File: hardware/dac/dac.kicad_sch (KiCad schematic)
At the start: 18 parts

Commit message: DAC layout almost done
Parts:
- removed C?: 0.1uF, symbol Device:C_Small
- removed U? (x3): 74LS139, symbol 74xx:74LS139
- removed U? (x2): 74LS04, symbol 74xx:74LS04
- added BT1: Battery_Cell, Connector_PinHeader_2.54mm:PinHeader_1x02_P2.54mm_Vertical, symbol Device:Battery_Cell
- added C11, C16, C2, C3, C4, C5, C6, C7, C8, C9: 0.1uF, Capacitor_THT:C_Disc_D3.4mm_W2.1mm_P2.50mm, symbol Device:C_Small
- added C14, C15: 33uF, Capacitor_THT:CP_Radial_D5.0mm_P2.00mm, symbol Device:C_Polarized_Small
- added C17, C18: 3.3uF 10V, Capacitor_THT:CP_Radial_D5.0mm_P2.50mm, symbol Device:C_Polarized_Small
- added D1, D2, D3: LED, LED_THT:LED_D3.0mm, symbol Device:LED
- added H1, H2, H3, H4: MountingHole, MountingHole:MountingHole_3.2mm_M3, symbol Mechanical:MountingHole
- added IC1: EC1110120201_with_knurled_SHAFT, ShaftEnc:EC1110120201withknurledSHAFT, symbol EC1110120201_with_knurled_SHAF:EC1110120201_with_knurled_SHAFT
- added J1, J7: Conn_01x04, Connector_PinHeader_2.54mm:PinHeader_1x04_P2.54mm_Vertical, symbol Connector_Generic:Conn_01x04
- added J4: Conn_02x08_Odd_Even, Connector_PinHeader_2.54mm:PinHeader_2x08_P2.54mm_Vertical, symbol Connector_Generic:Conn_02x08_Odd_Even
- added J5: Conn_01x02, Connector_PinHeader_2.54mm:PinHeader_1x02_P2.54mm_Vertical, symbol Connector_Generic:Conn_01x02
- added Q1: Q_PNP_BCE, Package_TO_SOT_THT:TO-92, symbol Device:Q_PNP_BCE
- added R1, R2, R3: R_US, Resistor_THT:R_Axial_DIN0207_L6.3mm_D2.5mm_P10.16mm_Horizontal, symbol Device:R_US
- added R4, R7: 10k, Resistor_THT:R_Axial_DIN0207_L6.3mm_D2.5mm_P10.16mm_Horizontal, symbol Device:R_US
- added R5, R6: 1k, Resistor_THT:R_Axial_DIN0207_L6.3mm_D2.5mm_P10.16mm_Horizontal, symbol Device:R_US
- added SW1, SW2: SW_SPST, Connector_PinHeader_2.54mm:PinHeader_1x02_P2.54mm_Vertical, symbol Switch:SW_SPST
- added U1: 74HC4040, Package_DIP:DIP-16_W7.62mm, symbol 4xxx:4040
- added unit 2 of U2
- added U3: 74LS174, Package_DIP:DIP-16_W7.62mm, symbol 74xx:74LS174
- added U5: 74LS138, Package_DIP:DIP-16_W7.62mm, symbol 74xx:74LS138
- added U6: DS1306, Package_DIP:DIP-16_W7.62mm, symbol DS1306:DS1306
- added U9: MAX503, Package_DIP:DIP-24_W7.62mm, symbol MAX530:MAX530
- added X1: 4.9152MHz, Oscillator:Oscillator_DIP-8, symbol Oscillator:CXO_DIP8
- added Y1: 32.768 kHz, Crystal:Crystal_C26-LF_D2.1mm_L6.5mm_Horizontal, symbol Device:Crystal
- C1, C10: renamed from C?; footprint (none) -> Capacitor_THT:C_Disc_D3.4mm_W2.1mm_P2.50mm; CatNo (none) -> 399-9859-1-ND
- C12, C13: renamed from C?; value C_Small -> 0.1uF; footprint (none) -> Capacitor_THT:C_Disc_D3.4mm_W2.1mm_P2.50mm; CatNo (none) -> 399-9859-1-ND
- J2, J3: renamed from J?; footprint (none) -> Connector_PinHeader_2.54mm:PinHeader_2x08_P2.54mm_Vertical
- J6: renamed from J?; footprint (none) -> Connector_PinHeader_2.54mm:PinHeader_1x04_P2.54mm_Horizontal
- U2: renamed from U?; footprint (none) -> Package_DIP:DIP-14_W7.62mm; CatNo (none) -> 296-1633-5-ND
- U4: renamed from U?; value 74LS245 -> 74HCT245; footprint (none) -> Package_DIP:DIP-20_W7.62mm; CatNo (none) -> 296-1612-5-ND
- U7: renamed from U?; footprint (none) -> Package_DIP:DIP-40_W15.24mm; CatNo (none) -> 2156-HD3-6402C-9-ND
- U8: renamed from U?; value MAX530 -> MAX503; footprint (none) -> Package_DIP:DIP-24_W7.62mm; CatNo (none) -> MAX503CNG+-ND
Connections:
- net +5V: now also U7.34 (CRL), U7.35 (PI), U7.37 (CLS2), U7.38 (CLS1), U8.15 (nCLR), U8.23 (VDD), C16.1, C17.1, C2.1, C3.1, C4.1, C6.1, C7.1, C9.1, D1.2 (A), D2.2 (A), D3.2 (A), J1.1 (Pin_1), Q1.3 (E), R7.2, U1.16 (VDD), U2.4, U3.16 (VCC), U5.16 (VCC), U5.6 (E3), U6.14 (VCCIF), U6.16 (VCC), U6.9 (SERMODE), U9.15 (nCLR), U9.23 (VDD), X1.8 (Vcc)
- net A0: now also U2.5
- net BD0: now also U8.24 (D0/D8), U3.3 (D0), U6.12 (SDI), U9.24 (D0/D8); no longer U7.38 (CLS1)
- net BD1: now also U8.1 (D1/D9), U3.4 (D1), U9.1 (D1/D9); no longer U7.37 (CLS2)
- net BD2: now also U8.2 (D2/D10), U3.6 (D2), U9.2 (D2/D10); no longer U7.36 (SBS)
- net BD3: now also U8.3 (D3/D11), U3.11 (D3), U9.3 (D3/D11); no longer U7.39 (EPE)
- net BD4: now also U8.4 (D4), U3.13 (D4), U9.4 (D4); no longer U7.35 (PI)
- net BD5: now also U8.5 (D5), U3.14 (D5), U9.5 (D5)
- net BD6: now also U8.6 (D6), U9.6 (D6)
- net BD7: now also U8.7 (D7), U9.7 (D7)
- net GND: now also J6.4 (Pin_4), U7.36 (SBS), U7.39 (EPE), U8.11 (nCS), U8.12 (DGND), U8.14 (AGND), U8.16 (nLDAC), U8.17 (REFGND), BT1.2 (-), C11.2, C14.2, C15.2, C16.2, C17.2, C18.1, C2.2, C3.2, C4.2, C5.2, C6.2, C7.2, C8.2, C9.2, IC1.C1 (WIPER), IC1.D1 (COM), J1.2 (Pin_2), J1.4 (Pin_4), J7.2 (Pin_2), J7.4 (Pin_4), SW1.1 (A), SW2.1 (A), U1.11 (Reset), U1.8 (VSS), U3.8 (GND), U5.5 (E2), U5.8 (GND), U6.1 (VCC2), U6.8 (GND), U9.11 (nCS), U9.16 (nLDAC), X1.4 (GND)
- net KD0: now also IC1.A1 (CCW)
- net KD1: now also IC1.B1 (CW)
- net KD2: now also IC1.E1 (NO)
- net KD3: now also SW1.2 (B)
- net KD4: now also SW2.2 (B); no longer J3.5 (Pin_5)
- net KD5: now also U6.13 (SDO)
- net KQ0: now also U5.1 (A0)
- net KQ1: now also U5.3 (A2)
- net KQ2: now also R4.1, R7.1
- net KQ3: now also U7.21 (MR)
- net KQ4: now also U6.10 (CE)
- net RXD: now also J6.2 (Pin_2)
- net TXD: now also J6.3 (Pin_3)
- net nLED1: now also U5.4 (E1)
- net nLED2: now also U6.11 (SCLK)
- net at U7.23 (nTBRL): now also U5.14 (O1)
- net at U7.18 (nDRR), U7.4 (RRD): now also U5.15 (O0)
- net at U7.16 (SFD): now also U5.13 (O2)
- net nDACX: now reaches U8.10 (nWR)
- net nDACX: now also U5.12 (O3)
- net at U8.13 (REFIN): now also U8.18 (REFOUT), U8.22 (ROFS), C14.1
- net -5V: now reaches U8.19 (VSS)
- net -5V: now also C11.1, C18.2, C5.1, C8.1, J1.3 (Pin_3), J5.2 (Pin_2), U9.19 (VSS)
- net at U8.20 (VOUT): now also U8.21 (RFB), R5.1
- net BA0: now reaches U8.8 (A0)
- net BA0: now also U8.9 (A1), U2.6, U5.2 (A1), U9.8 (A0), U9.9 (A1)
- net CLK16X: now reaches U7.17 (RRC)
- net CLK16X: now also U7.40 (TRC), J4.10 (Pin_10), J4.12 (Pin_12), J4.14 (Pin_14), J4.16 (Pin_16), J4.2 (Pin_2), J4.4 (Pin_4), J4.6 (Pin_6), J4.8 (Pin_8)
- new net: D1.1 (K), R1.2
- new net: D3.1 (K), R3.2
- new net: J5.1 (Pin_1), Q1.2 (C)
- new net: C15.1, U9.13 (REFIN), U9.18 (REFOUT), U9.22 (ROFS)
- new net: Q1.1 (B), R4.2
- new net: R6.1, U9.20 (VOUT), U9.21 (RFB)
- new net: BT1.1 (+), U6.2 (VBAT)
- new net: U6.3 (X1), Y1.1
- new net: U6.4 (X2), Y1.2
- new net: D2.1 (K), R2.2
- new net: U1.10 (CLK), X1.5 (OUT)
- new net: U9.12 (DGND), U9.14 (AGND), U9.17 (REFGND)
- new net B1200: J4.11 (Pin_11), U1.13 (Q7)
- new net B19200: J4.3 (Pin_3), U1.5 (Q3)
- new net B2400: J4.9 (Pin_9), U1.4 (Q6)
- new net B300: J4.15 (Pin_15), U1.14 (Q9)
- new net B38400: J4.1 (Pin_1), U1.6 (Q2)
- new net B4800: J4.7 (Pin_7), U1.2 (Q5)
- new net B600: J4.13 (Pin_13), U1.12 (Q8)
- new net B9600: J4.5 (Pin_5), U1.3 (Q4)
- new net LED0: R1.1, U3.2 (Q0)
- new net LED1: R2.1, U3.5 (Q1)
- new net LED2: R3.1, U3.7 (Q2)
- new net LED3: U3.10 (Q3)
- new net LED4: U3.12 (Q4)
- new net LED5: U3.15 (Q5)
- new net X_OUT: J7.1 (Pin_1), R6.2
- new net Y_OUT: J7.3 (Pin_3), R5.2
- new net nDACY: U5.10 (O5), U9.10 (nWR)
- new net nEXP: U3.9 (Cp), U5.7 (O7)
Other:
- note added: "8 bits, no parity 1 stop bit"
- note added: "Baud Rate Generator"
- note added: "CRT Z axis drive"
- note added: "Even: RD Odd: WR"
- note added: "Input Bits: KD0 - encoder A KD1 - encoder B KD2 - encoder SW KD3 - button 1 KD4 - button 2 KD5 - RTC Serial Data KD6 - Spare"
- note added: "Primiary Outputs KQ0 dir H=WR KQ1 dev sel 0 KQ2 Z enable KQ3 UART reset KQ4 RTC CE"
- note added: "RD"
- note added: "Real-Time Clock"
- note added: "Shaft Encoder"
- note added: "Sparkfun BOB-12731 USB - FT232RL"
- note added: "UART"
- note added: "WR"
- note removed: "CTRL LOAD"
- note removed: "FT232 breakout"
- moved on the sheet: C1, C10, J6, U2A, U2E, U8

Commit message: PCB Rev 1 ready to fab?
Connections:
- net +5V: now also U3.1 (~{Mr})
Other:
- note added: "Scope Clock DAQ/Control Interface"
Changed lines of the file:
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@@
     (stroke (width 0) (type default) (color 0 0 0 0))
   )
+  (wire (pts (xy 85.09 191.77) (xy 87.63 191.77))
+    (stroke (width 0) (type default) (color 0 0 0 0))
+  )
   (wire (pts (xy 113.03 181.61) (xy 120.65 181.61))
     (stroke (width 0) (type default) (color 0 0 0 0))
@@
     (effects (font (size 1.27 1.27)) (justify left bottom))
   )
+  (text "Scope Clock DAQ/Control Interface" (at 161.29 180.34 0)
+    (effects (font (size 2.54 2.54)) (justify left bottom))
+  )
   (text "Real-Time Clock" (at 123.19 113.03 0)
     (effects (font (size 1.905 1.905)) (justify left bottom))
@@
     (pin "1")
   )
+  (symbol (lib_id "power:+5V") (at 85.09 191.77 0) (unit 1)
+    (in_bom yes) (on_board yes)
+    (property "Reference" "#PWR?" (id 0) (at 85.09 195.58 0)
+      (effects (font (size 1.27 1.27)) hide)
+    )
+    (property "Value" "+5V" (id 1) (at 81.28 190.5 0))
+    (property "Footprint" "" (id 2) (at 85.09 191.77 0)
+      (effects (font (size 1.27 1.27)) hide)
+    )
+    (property "Datasheet" "" (id 3) (at 85.09 191.77 0)
+      (effects (font (size 1.27 1.27)) hide)
+    )
+    (pin "1")
+  )
   (symbol (lib_id "power:GND") (at 110.49 109.22 0) (unit 1)
     (in_bom yes) (on_board yes)
@@
       (reference "#PWR053") (unit 1) (value "GND") (footprint "")
     )
+    (path "/12f4a369-d6ff-4aa1-ab4f-7a5c25ac096c"
+      (reference "#PWR?") (unit 1) (value "+5V") (footprint "")
+    )
     (path "/7e11c5d6-00d5-4ef8-b7e7-4746244c75fa"

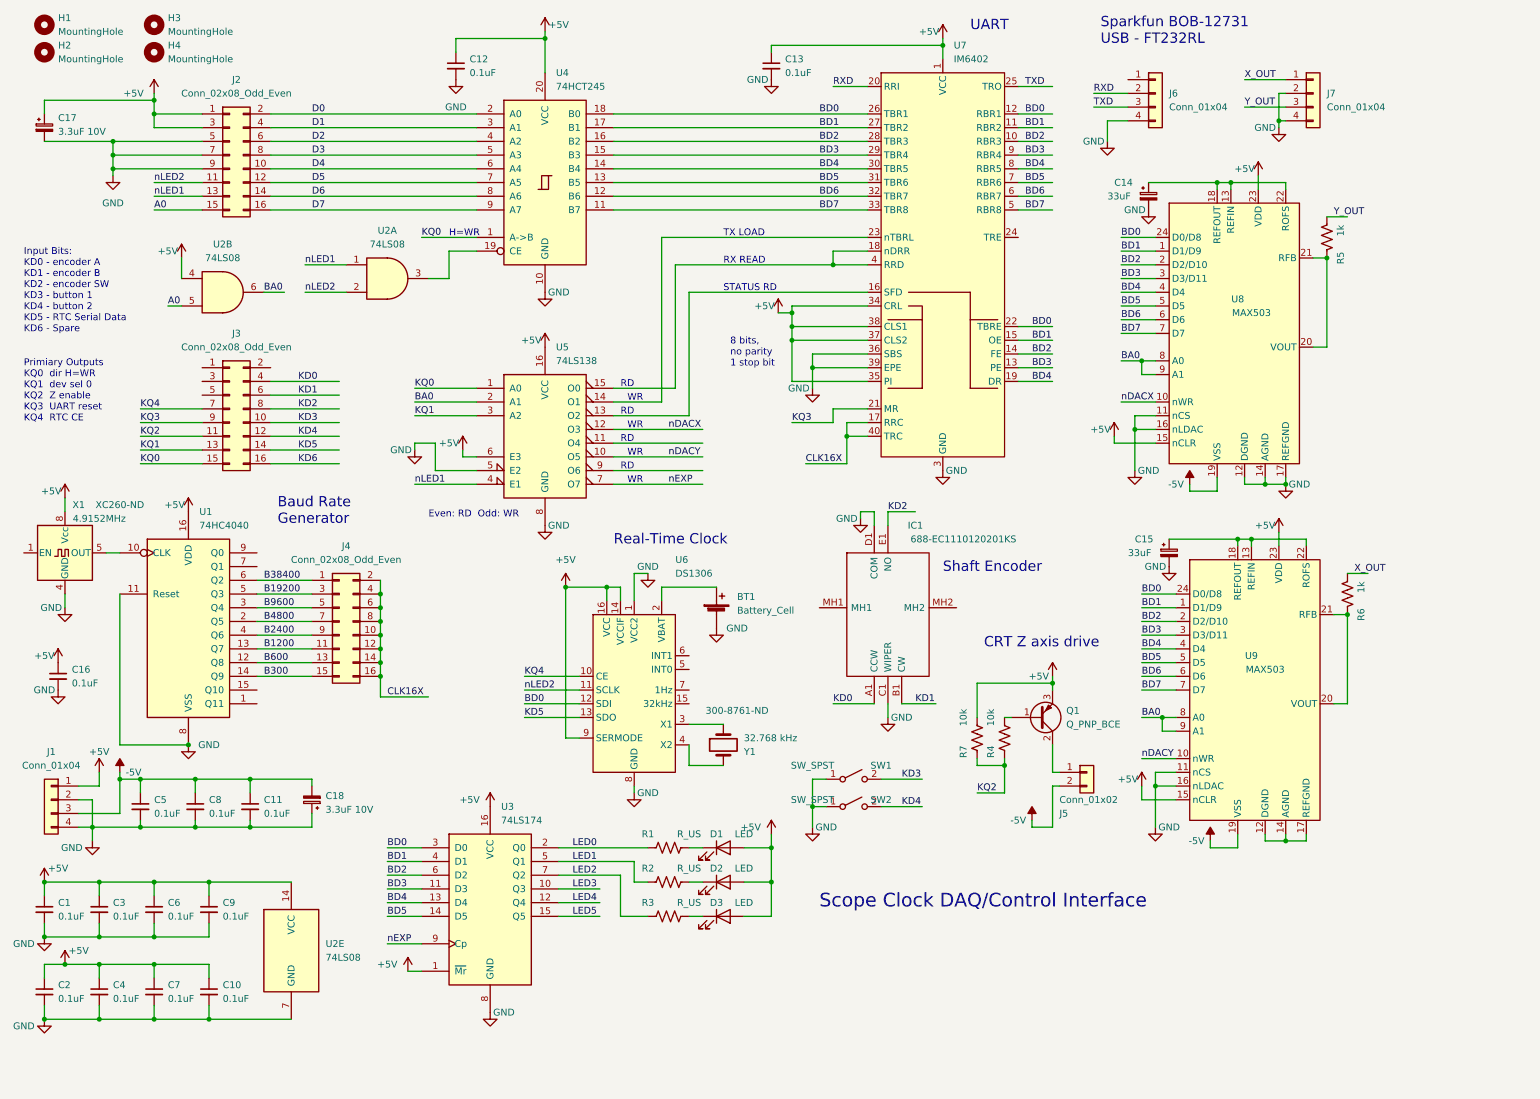
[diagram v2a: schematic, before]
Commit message: working on Rev 2 DAC
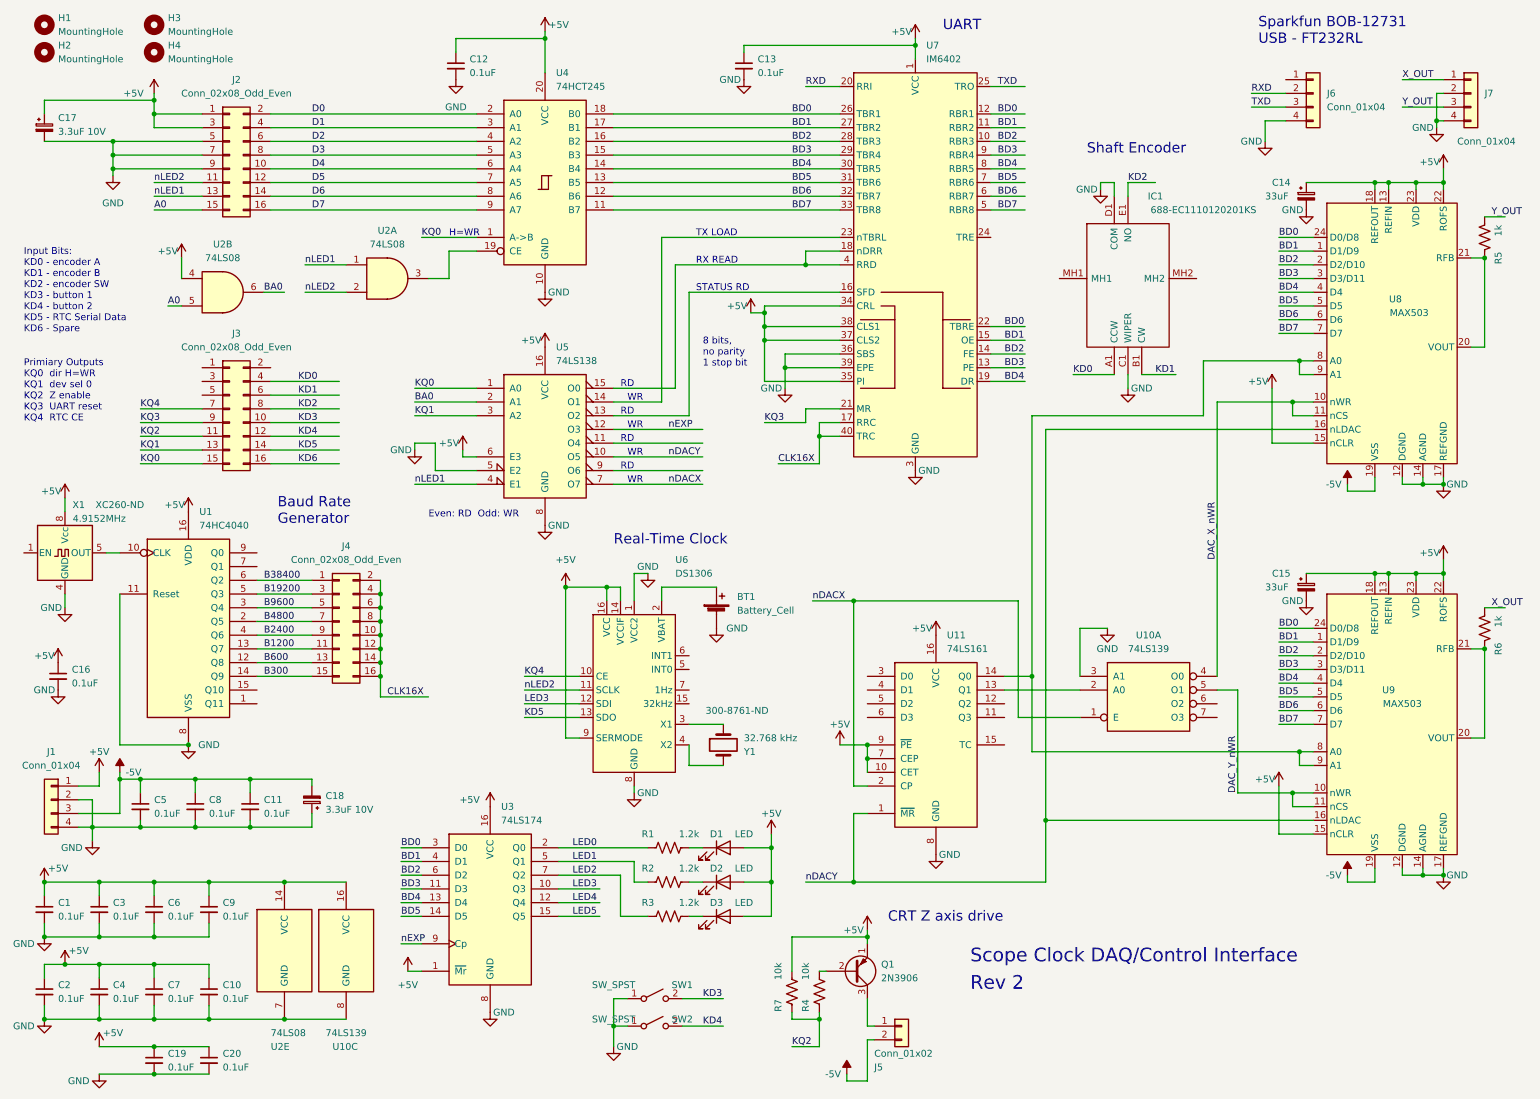
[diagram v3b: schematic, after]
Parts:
- added C19, C20: 0.1uF, Capacitor_THT:C_Disc_D3.4mm_W2.1mm_P2.50mm, symbol Device:C_Small
- added U10: 74LS139, Package_DIP:DIP-16_W7.62mm, symbol 74xx:74LS139
- added U11: 74LS161, Package_DIP:DIP-16_W7.62mm, symbol 74xx:74LS161
- C17, C18: CatNo (none) -> 10-EEU-FC1H3R3HCT-ND
- Q1: value Q_PNP_BCE -> 2N3906; symbol Device:Q_PNP_BCE -> Device:Q_PNP_EBC
- R1, R2, R3: value R_US -> 1.2k
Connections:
- net +5V: now also C14.1, C15.1, Q1.1 (E), U8.13 (REFIN), U8.18 (REFOUT), U8.22 (ROFS), U9.13 (REFIN), U9.18 (REFOUT), U9.22 (ROFS), C19.1, C20.1, U10.16 (VCC), U11.10 (CET), U11.16 (VCC), U11.7 (CEP), U11.9 (~{PE}); no longer Q1.3 (E)
- net BA0: no longer U8.8 (A0), U8.9 (A1), U9.8 (A0), U9.9 (A1)
- net BD0: no longer U6.12 (SDI)
- net GND: now also U9.12 (DGND), U9.14 (AGND), U9.17 (REFGND), C19.2, C20.2, U10.3 (A1), U10.8 (GND), U11.8 (GND); no longer U8.11 (nCS), U8.16 (nLDAC), U9.11 (nCS), U9.16 (nLDAC)
- net LED3: now also U6.12 (SDI)
- net nDACX: now also U5.7 (O7), U10.1 (E), U11.2 (CP); no longer U5.12 (O3), U8.10 (nWR)
- net nDACY: now also U8.16 (nLDAC), U9.16 (nLDAC), U11.1 (~{MR}); no longer U9.10 (nWR)
- net nEXP: now also U5.12 (O3); no longer U5.7 (O7)
- net at J5.1 (Pin_1): now also Q1.3 (C); no longer Q1.2 (C)
- net at R4.2: now also Q1.2 (B); no longer Q1.1 (B)
- new net: U11.14 (Q0), U8.8 (A0), U8.9 (A1), U9.8 (A0), U9.9 (A1)
- new net: U10.2 (A0), U11.13 (Q1)
- new net DAC_X_nWR: U10.4 (O0), U8.10 (nWR), U8.11 (nCS)
- new net DAC_Y_nWR: U10.5 (O1), U9.10 (nWR), U9.11 (nCS)
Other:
- note added: "Rev 2"
- moved on the sheet: C13, C14, C15, IC1, J5, J6, J7, Q1, R4, R5, R6, R7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

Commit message: software tweaks, working on case
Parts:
- removed IC1: EC1110120201_with_knurled_SHAFT, ShaftEnc:EC1110120201withknurledSHAFT, symbol EC1110120201_with_knurled_SHAF:EC1110120201_with_knurled_SHAFT
- added J8: Conn_01x02, Connector_PinHeader_2.54mm:PinHeader_1x02_P2.54mm_Vertical, symbol Connector_Generic:Conn_01x02
- added SW3: EN11-VSM1AF20, footprints:SWITCH_VSM1AF20_BIT, symbol Device:RotaryEncoder_Switch
- SW1, SW2: footprint Connector_PinHeader_2.54mm:PinHeader_1x02_P2.54mm_Vertical -> Button_Switch_THT:SW_Push_1P2T_Vertical_E-Switch_800UDP8P1A1M6; symbol Switch:SW_SPST -> my_sw:SW_SPST_1_3; CatNo (none) -> EG2615-ND
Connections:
- net GND: now also J8.2 (Pin_2), SW3.C, SW3.E (S2)
- net KD0: now also SW3.D (S1)
- net KD1: now also SW3.A
- net KD2: now also SW3.B
- net KD3: now also SW1.3 (B); no longer SW1.2 (B)
- net KD4: now also SW2.3 (B); no longer SW2.2 (B)
- net LED4: now also J8.1 (Pin_1)
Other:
- note added: "HV Enable"
- note added: "Pushbuttons"
- moved on the sheet: SW1, SW2

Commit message: gerbers as built (DAC), 3D case wide version
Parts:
- C1, C10, C11, C12, C13, C14, C15, C16, C17, C18, C19, C2, C20, C3, C4, C5, C6, C7, C8, C9, U1, U10, U11, U2, U3, U4, U5, U8, U9, Y1: DNP (none) -> Y

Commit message: schematic notes
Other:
- note added: "Input Bits: KD0 - encoder SW KD1 - encoder A KD2 - encoder B KD3 - button 1 KD4 - button 2 KD5 - RTC Serial Data KD6 - Spare"
- note removed: "Input Bits: KD0 - encoder A KD1 - encoder B KD2 - encoder SW KD3 - button 1 KD4 - button 2 KD5 - RTC Serial Data KD6 - Spare"
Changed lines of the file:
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@@
     (effects (font (size 1.905 1.905)) (justify left bottom))
   )
-  (text "Input Bits:\nKD0 - encoder A\nKD1 - encoder B\nKD2 - encoder SW\nKD3 - button 1\nKD4 - button 2\nKD5 - RTC Serial Data\nKD6 - Spare"
+  (text "Input Bits:\nKD0 - encoder SW\nKD1 - encoder A\nKD2 - encoder B\nKD3 - button 1\nKD4 - button 2\nKD5 - RTC Serial Data\nKD6 - Spare"
     (at 13.97 73.66 0)
     (effects (font (size 1.27 1.27)) (justify left bottom))
